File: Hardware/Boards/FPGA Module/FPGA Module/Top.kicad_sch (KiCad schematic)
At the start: 0 parts

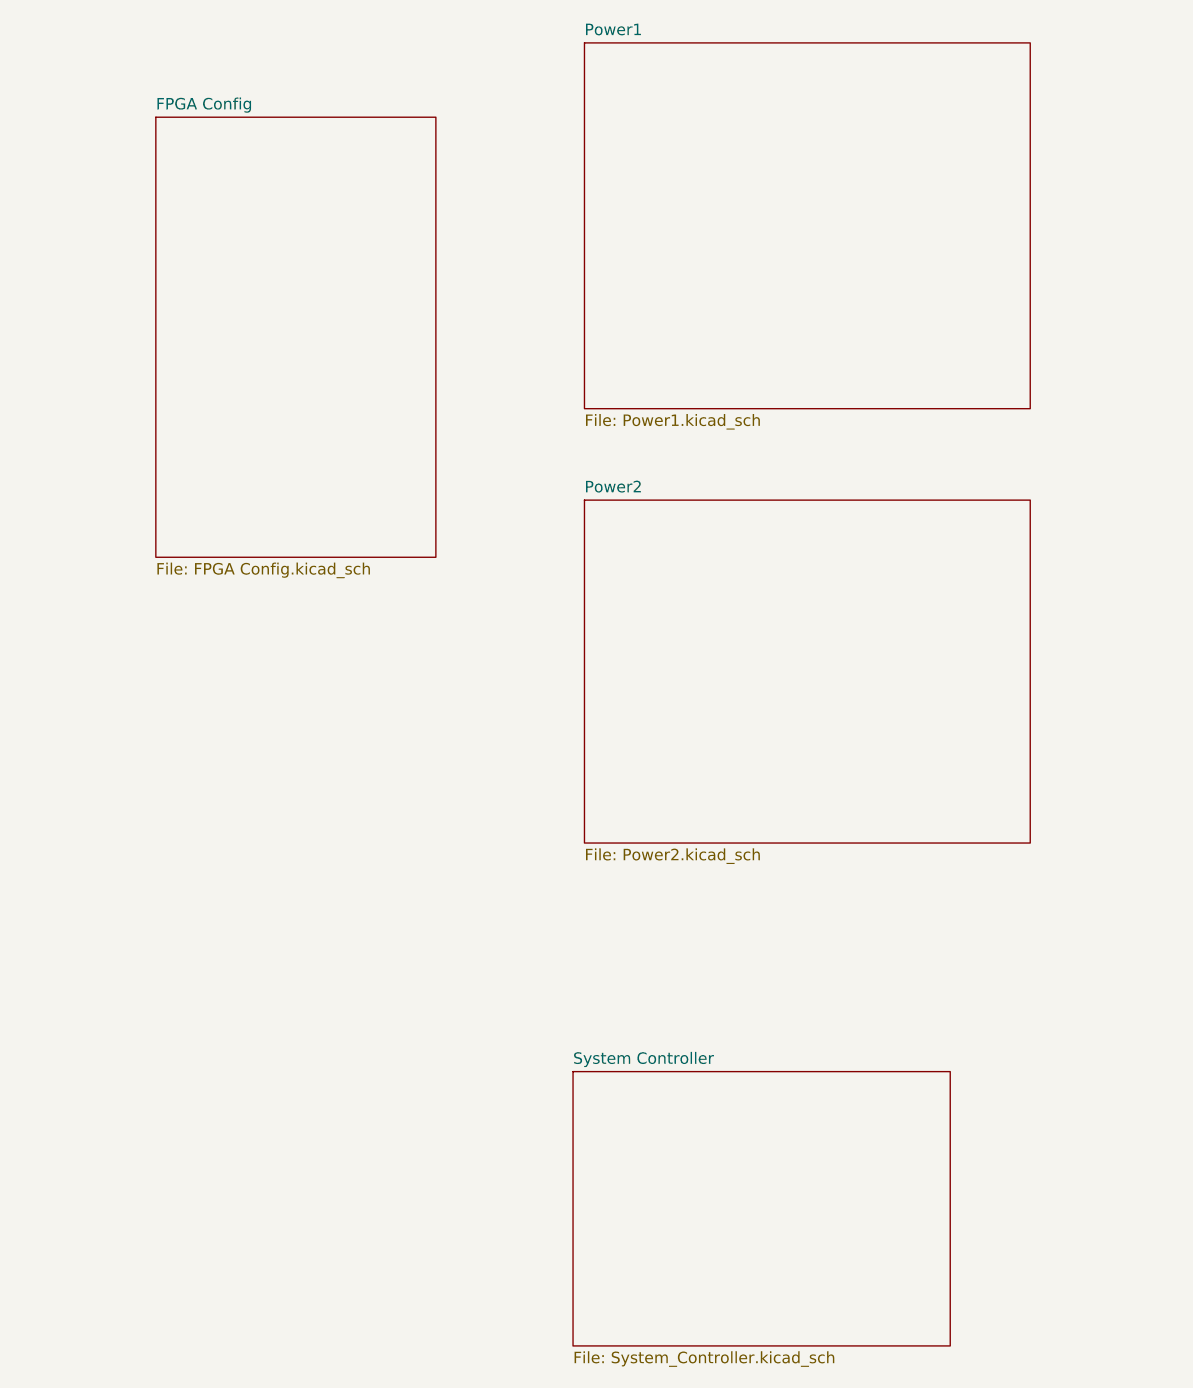
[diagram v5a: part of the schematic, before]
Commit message: updated fpga module schematics
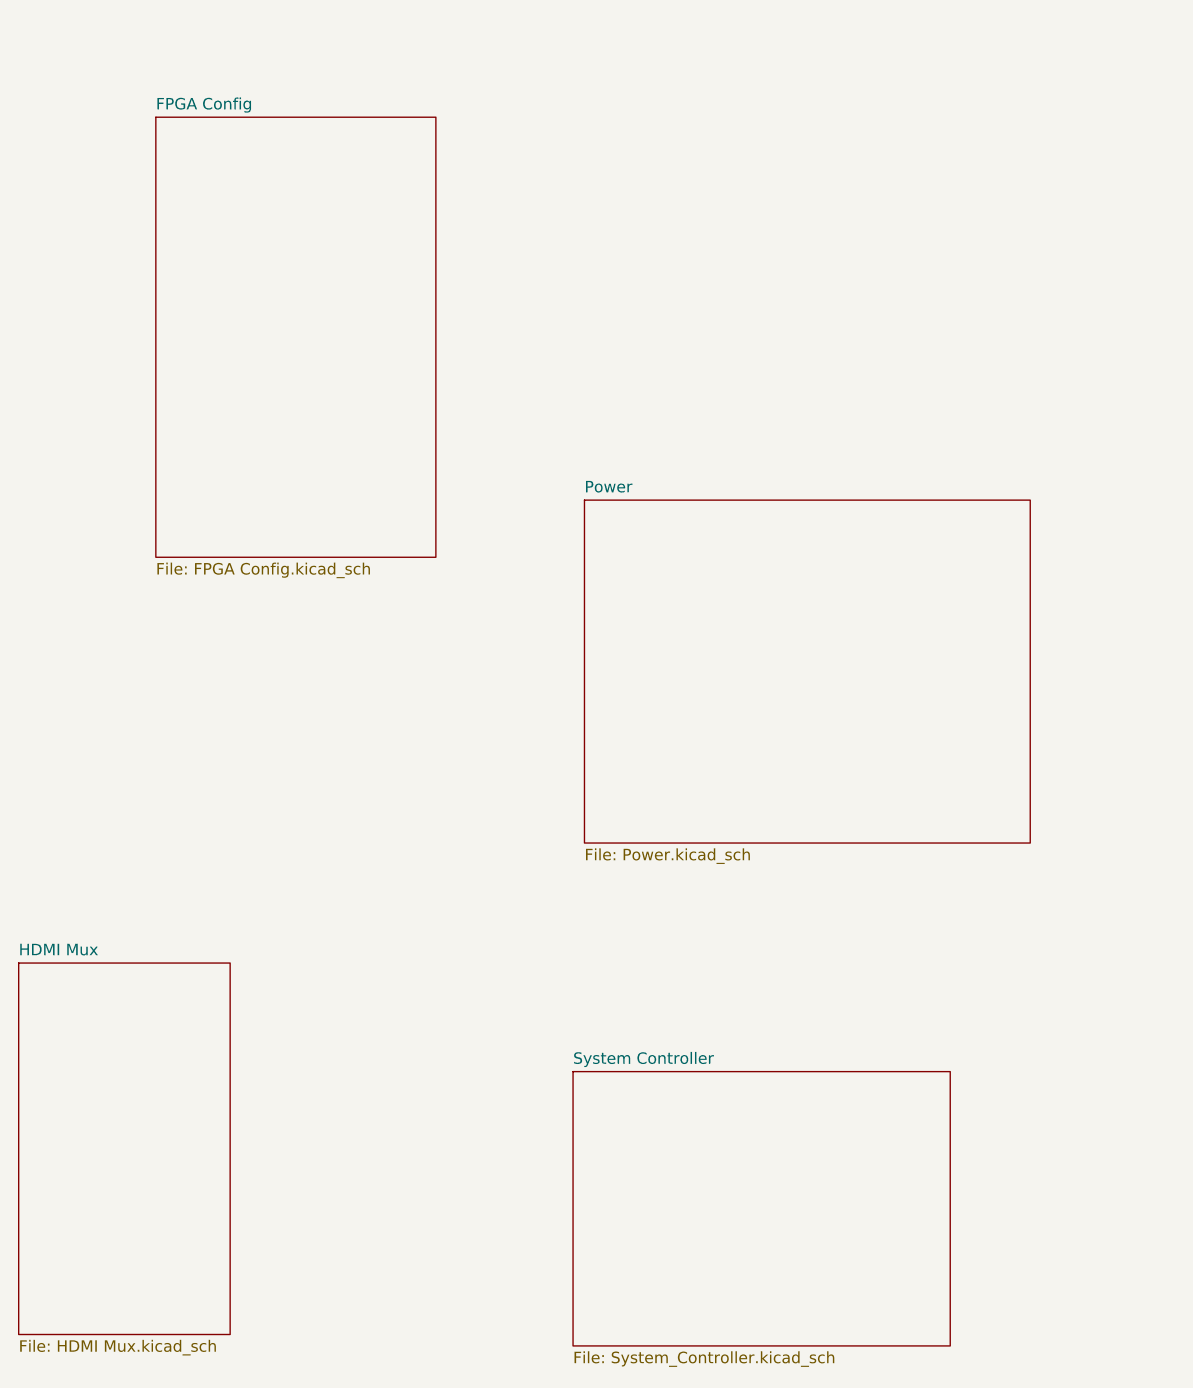
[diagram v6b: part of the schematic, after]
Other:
- sheet Power2 renamed Power
- removed sheet Power1
- added sheet HDMI Mux (HDMI Mux.kicad_sch)
- sheet Power: file Power2.kicad_sch -> Power.kicad_sch
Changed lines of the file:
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@@
 			(color 0 0 0 0.0000)
 		)
-		(property "Sheetname" "Power2"
+		(property "Sheetname" "Power"
 			(at 129.54 121.2084 0)
 			(effects
@@
 			)
 		)
-		(property "Sheetfile" "Power2.kicad_sch"
+		(property "Sheetfile" "Power.kicad_sch"
 			(at 129.54 160.6046 0)
 			(effects
@@
 	)
 	(sheet
-		(at 129.54 71.12)
-		(size 49.53 40.64)
+		(at 66.675 173.355)
+		(size 23.495 41.275)
 		(fields_autoplaced yes)
 		(stroke
@@
 			(color 0 0 0 0.0000)
 		)
-		(property "Sheetname" "Power1"
-			(at 129.54 70.4084 0)
+		(property "Sheetname" "HDMI Mux"
+			(at 66.675 172.6434 0)
 			(effects
 				(font
@@
 			)
 		)
-		(property "Sheetfile" "Power1.kicad_sch"
-			(at 129.54 112.3446 0)
+		(property "Sheetfile" "HDMI Mux.kicad_sch"
+			(at 66.675 215.2146 0)
 			(effects
 				(font
@@
 			(project "FPGA Module"
 				(path "/199f10e2-d4b4-4a27-9e84-7b1ce2ae6bf0/0c296310-f788-47f0-8a3f-43c3444563e8"
-					(page "8")
+					(page "11")
 				)
 			)

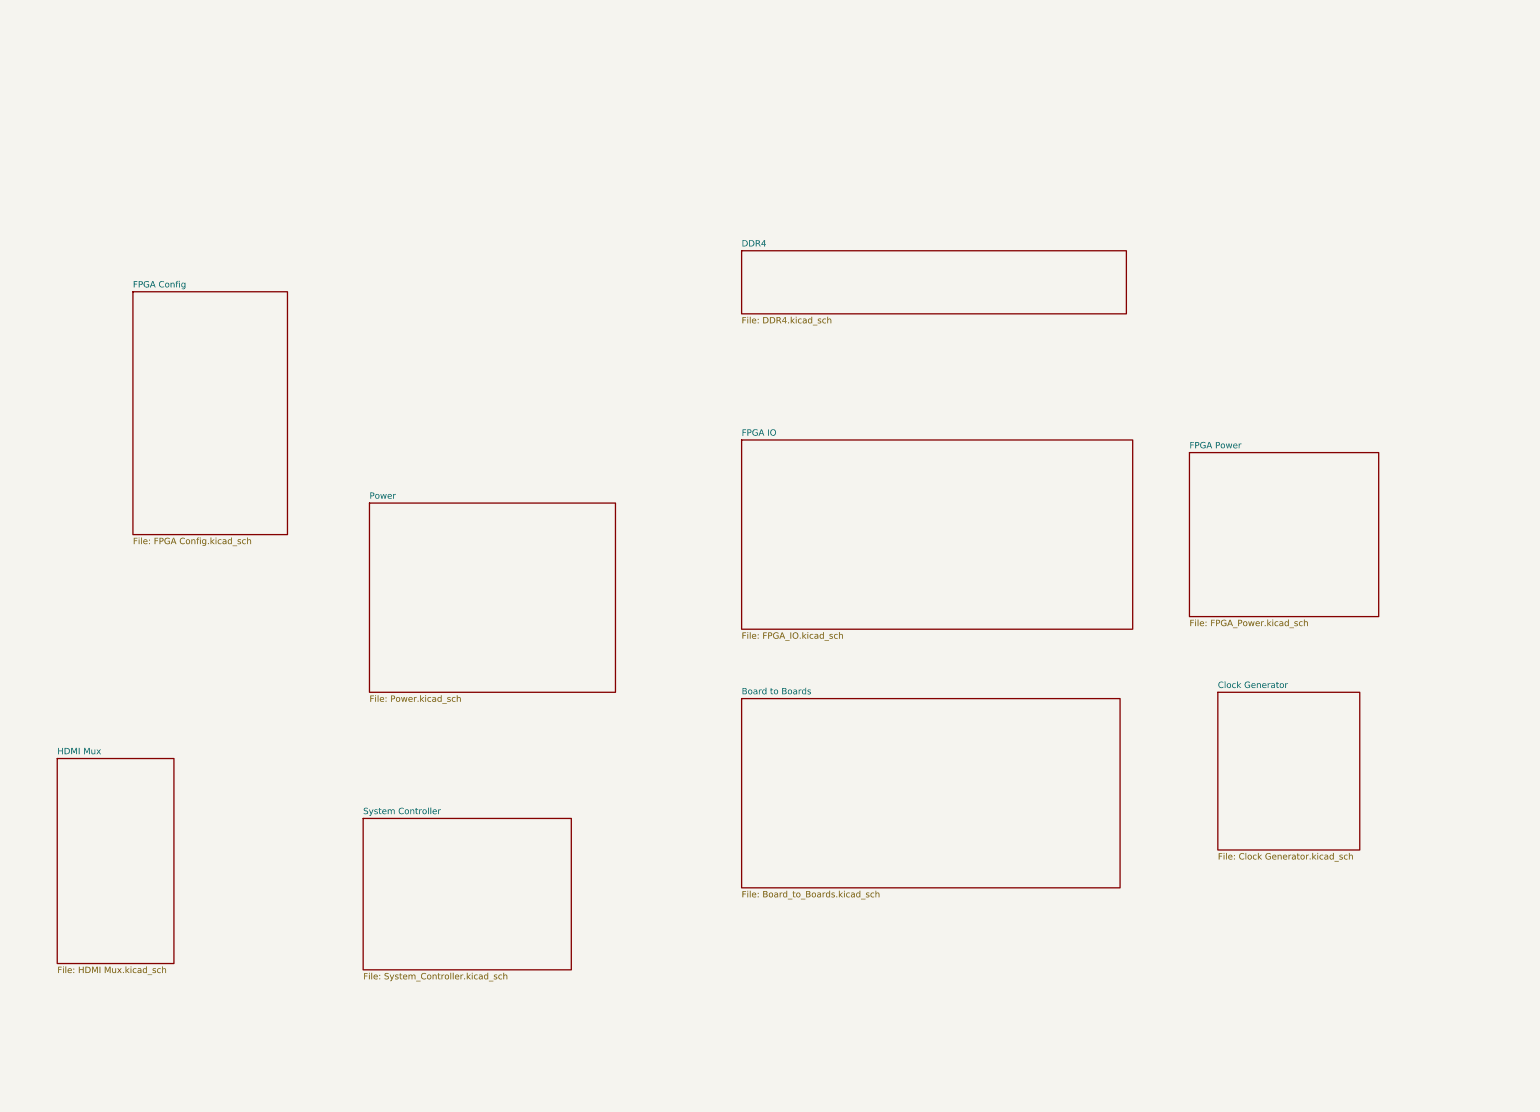
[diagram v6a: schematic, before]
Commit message: Added Top sheet connections for FPGA module
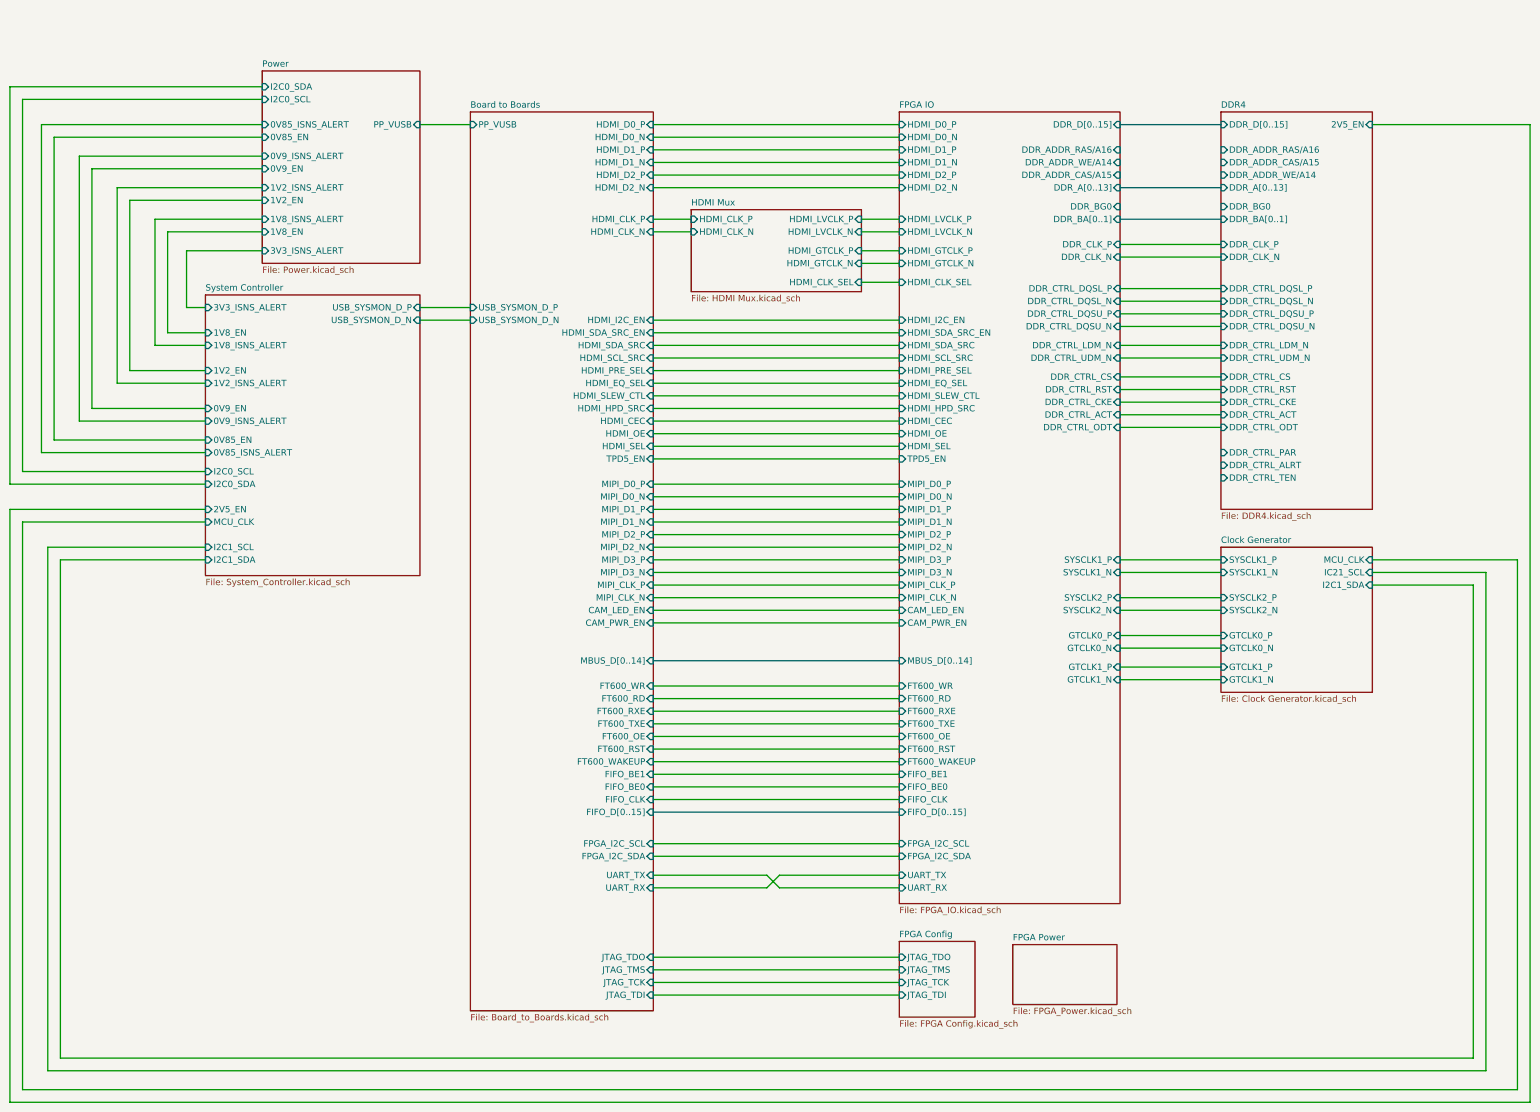
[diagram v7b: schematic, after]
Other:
- sheet Board to Boards ports: added CAM_LED_EN, CAM_PWR_EN, FIFO_BE0, FIFO_BE1, FIFO_CLK, FIFO_D[0..15], FPGA_I2C_SCL, FPGA_I2C_SDA, FT600_OE, FT600_RD, FT600_RST, FT600_RXE, FT600_TXE, FT600_WAKEUP, FT600_WR, HDMI_CEC, HDMI_CLK_N, HDMI_CLK_P, HDMI_D0_N, HDMI_D0_P, HDMI_D1_N, HDMI_D1_P, HDMI_D2_N, HDMI_D2_P, HDMI_EQ_SEL, HDMI_HPD_SRC, HDMI_I2C_EN, HDMI_OE, HDMI_PRE_SEL, HDMI_SCL_SRC, HDMI_SDA_SRC, HDMI_SDA_SRC_EN, HDMI_SEL, HDMI_SLEW_CTL, JTAG_TCK, JTAG_TDI, JTAG_TDO, JTAG_TMS, MBUS_D[0..14], MIPI_CLK_N, MIPI_CLK_P, MIPI_D0_N, MIPI_D0_P, MIPI_D1_N, MIPI_D1_P, MIPI_D2_N, MIPI_D2_P, MIPI_D3_N, MIPI_D3_P, PP_VUSB, TPD5_EN, UART_RX, UART_TX, USB_SYSMON_D_N, USB_SYSMON_D_P; removed none
- sheet Clock Generator ports: added GTCLK0_N, GTCLK0_P, GTCLK1_N, GTCLK1_P, I2C1_SDA, IC21_SCL, MCU_CLK, SYSCLK1_N, SYSCLK1_P, SYSCLK2_N, SYSCLK2_P; removed none
- sheet DDR4 ports: added 2V5_EN, DDR_ADDR_CAS/A15, DDR_ADDR_RAS/A16, DDR_ADDR_WE/A14, DDR_A[0..13], DDR_BA[0..1], DDR_BG0, DDR_CLK_N, DDR_CLK_P, DDR_CTRL_ACT, DDR_CTRL_ALRT, DDR_CTRL_CKE, DDR_CTRL_CS, DDR_CTRL_DQSL_N, DDR_CTRL_DQSL_P, DDR_CTRL_DQSU_N, DDR_CTRL_DQSU_P, DDR_CTRL_LDM_N, DDR_CTRL_ODT, DDR_CTRL_PAR, DDR_CTRL_RST, DDR_CTRL_TEN, DDR_CTRL_UDM_N, DDR_D[0..15]; removed none
- sheet FPGA Config ports: added JTAG_TCK, JTAG_TDI, JTAG_TDO, JTAG_TMS; removed none
- sheet FPGA IO ports: added CAM_LED_EN, CAM_PWR_EN, DDR_ADDR_CAS/A15, DDR_ADDR_RAS/A16, DDR_ADDR_WE/A14, DDR_A[0..13], DDR_BA[0..1], DDR_BG0, DDR_CLK_N, DDR_CLK_P, DDR_CTRL_ACT, DDR_CTRL_CKE, DDR_CTRL_CS, DDR_CTRL_DQSL_N, DDR_CTRL_DQSL_P, DDR_CTRL_DQSU_N, DDR_CTRL_DQSU_P, DDR_CTRL_LDM_N, DDR_CTRL_ODT, DDR_CTRL_RST, DDR_CTRL_UDM_N, DDR_D[0..15], FIFO_BE0, FIFO_BE1, FIFO_CLK, FIFO_D[0..15], FPGA_I2C_SCL, FPGA_I2C_SDA, FT600_OE, FT600_RD, FT600_RST, FT600_RXE, FT600_TXE, FT600_WAKEUP, FT600_WR, GTCLK0_N, GTCLK0_P, GTCLK1_N, GTCLK1_P, HDMI_CEC, HDMI_CLK_SEL, HDMI_D0_N, HDMI_D0_P, HDMI_D1_N, HDMI_D1_P, HDMI_D2_N, HDMI_D2_P, HDMI_EQ_SEL, HDMI_GTCLK_N, HDMI_GTCLK_P, HDMI_HPD_SRC, HDMI_I2C_EN, HDMI_LVCLK_N, HDMI_LVCLK_P, HDMI_OE, HDMI_PRE_SEL, HDMI_SCL_SRC, HDMI_SDA_SRC, HDMI_SDA_SRC_EN, HDMI_SEL, HDMI_SLEW_CTL, MBUS_D[0..14], MIPI_CLK_N, MIPI_CLK_P, MIPI_D0_N, MIPI_D0_P, MIPI_D1_N, MIPI_D1_P, MIPI_D2_N, MIPI_D2_P, MIPI_D3_N, MIPI_D3_P, SYSCLK1_N, SYSCLK1_P, SYSCLK2_N, SYSCLK2_P, TPD5_EN, UART_RX, UART_TX; removed none
- sheet HDMI Mux ports: added HDMI_CLK_N, HDMI_CLK_P, HDMI_CLK_SEL, HDMI_GTCLK_N, HDMI_GTCLK_P, HDMI_LVCLK_N, HDMI_LVCLK_P; removed none
- sheet Power ports: added 0V85_EN, 0V85_ISNS_ALERT, 0V9_EN, 0V9_ISNS_ALERT, 1V2_EN, 1V2_ISNS_ALERT, 1V8_EN, 1V8_ISNS_ALERT, 3V3_ISNS_ALERT, I2C0_SCL, I2C0_SDA, PP_VUSB; removed none
- sheet System Controller ports: added 0V85_EN, 0V85_ISNS_ALERT, 0V9_EN, 0V9_ISNS_ALERT, 1V2_EN, 1V2_ISNS_ALERT, 1V8_EN, 1V8_ISNS_ALERT, 2V5_EN, 3V3_ISNS_ALERT, I2C0_SCL, I2C0_SDA, I2C1_SCL, I2C1_SDA, MCU_CLK, USB_SYSMON_D_N, USB_SYSMON_D_P; removed none

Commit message: Added NC to unused pins
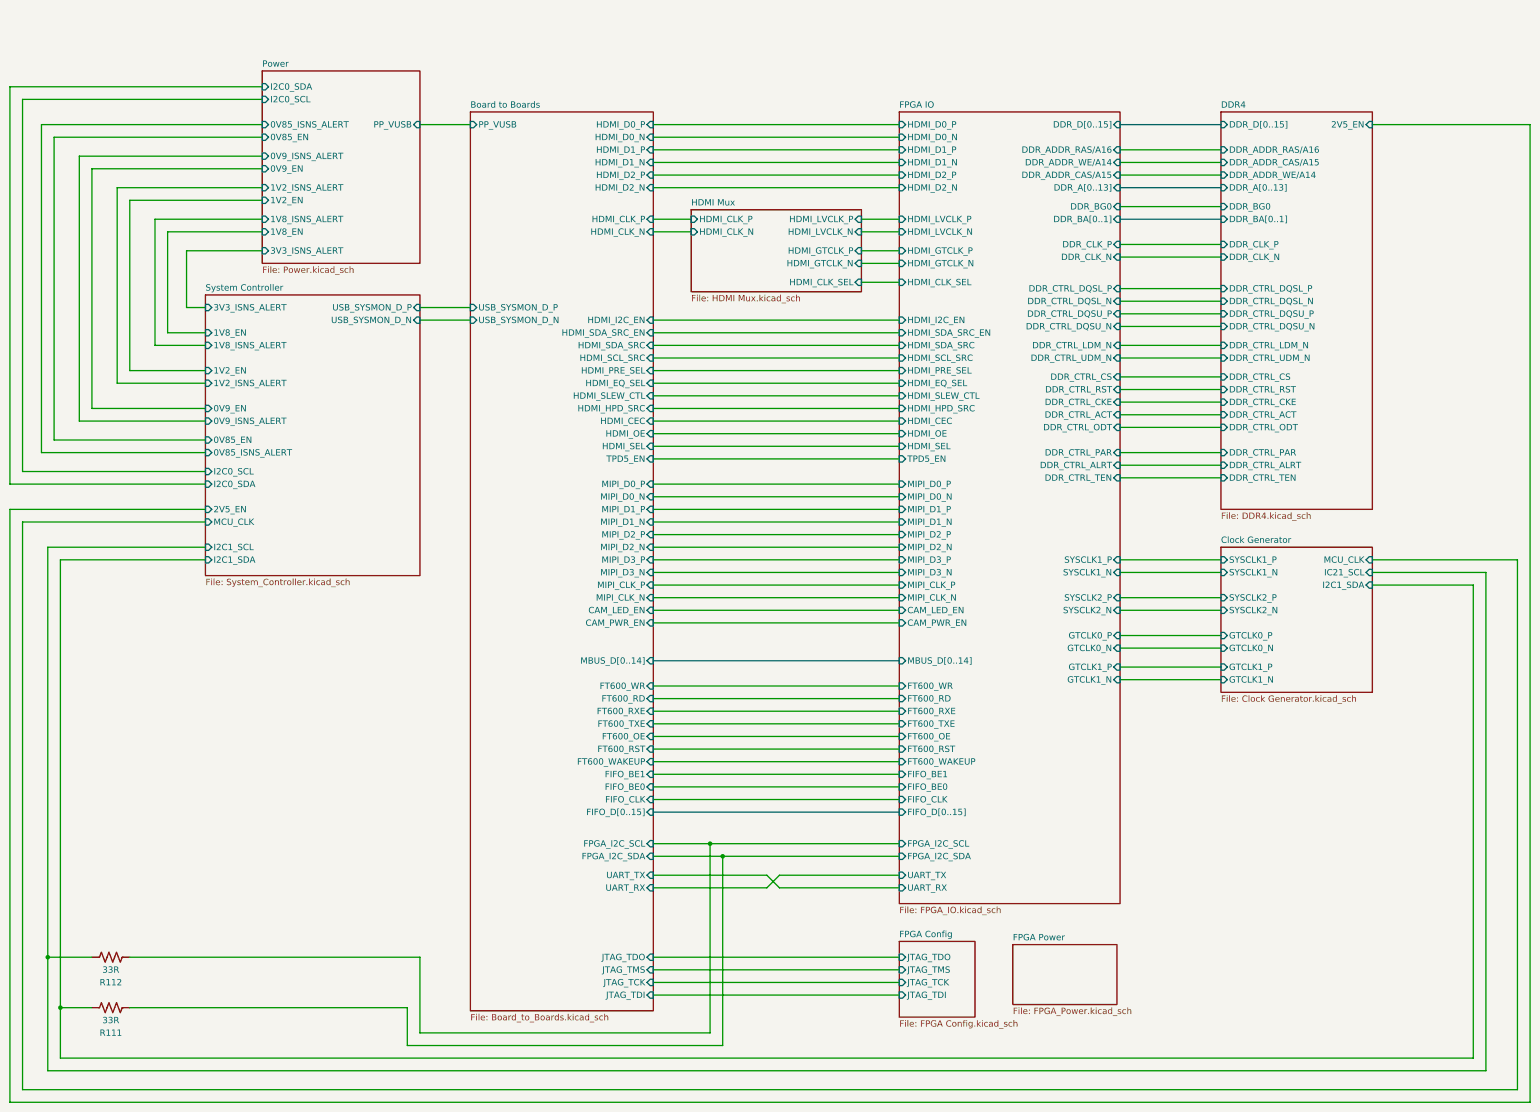
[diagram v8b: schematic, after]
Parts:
- added R111, R112: 33R, Resistor_SMD:R_0402_1005Metric, symbol Device:R_US
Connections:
- net Board to Boards/FPGA_I2C_SCL: now also R112.2
- net Board to Boards/FPGA_I2C_SDA: now also R111.2
- net Clock Generator/I2C1_SDA: now also R111.1
- net Clock Generator/IC21_SCL: now also R112.1
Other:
- sheet FPGA IO ports: added DDR_CTRL_ALRT, DDR_CTRL_PAR, DDR_CTRL_TEN; removed none
